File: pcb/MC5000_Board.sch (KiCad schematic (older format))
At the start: 0 parts

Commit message: Work on PCB
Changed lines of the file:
@@
 $Descr A4 11693 8268
 encoding utf-8
-Sheet 1 9
+Sheet 1 10
 Title ""
 Date ""
@@
 $EndSheet
 $Sheet
-S 750  750  1750 1100
+S 2650 3700 1600 1050
 U 602FB936
-F0 "PFS172 breakout - Display Controller" 50
+F0 "PFS172 breakout - Display Ctrl" 50
 F1 "PFS172_breakout.sch" 50
 $EndSheet
 $Sheet
-S 2850 750  1600 1100
+S 750  750  1600 1100
 U 60303416
 F0 "PFS172 breakout - MCU1" 50
@@
 $EndSheet
 $Sheet
-S 750  2200 1750 1050
+S 2650 800  1600 1050
 U 6030344A
 F0 "PFS172 breakout - MCU2" 50
@@
 $EndSheet
 $Sheet
-S 2850 2200 1600 1050
+S 750  2200 1600 1050
 U 603034BC
 F0 "PFS172 breakout - MCU3" 50
@@
 $EndSheet
 $Sheet
-S 750  3700 1750 1050
+S 750  3700 1600 1050
 U 60318BF9
-F0 "PFS172 extra #1" 50
+F0 "PFS172 Buzzer Ctrl" 50
 F1 "PFS172_breakout.sch" 50
 $EndSheet
 $Sheet
-S 2850 3700 1600 1050
+S 2650 2200 1600 1050
 U 60318BFB
-F0 "PFS172 extra #2" 50
+F0 "PFS172 extra" 50
 F1 "PFS172_breakout.sch" 50
 $EndSheet
+$Sheet
+S 800  6400 1550 1050
+U 6034DF24
+F0 "MCU5000 #1" 50
+F1 "MCU5000.sch" 50
+$EndSheet
 $EndSCHEMATC

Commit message: Added buzzer
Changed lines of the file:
@@
 $Descr A4 11693 8268
 encoding utf-8
-Sheet 1 10
+Sheet 1 12
 Title ""
 Date ""
@@
 F1 "MCU5000.sch" 50
 $EndSheet
+$Sheet
+S 2700 6400 1550 1050
+U 603599D1
+F0 "MCU5000 #2" 50
+F1 "MCU5000.sch" 50
+$EndSheet
+$Sheet
+S 8500 700  1700 1000
+U 603632C9
+F0 "Buzzer" 50
+F1 "buzzer.sch" 50
+$EndSheet
 $EndSCHEMATC

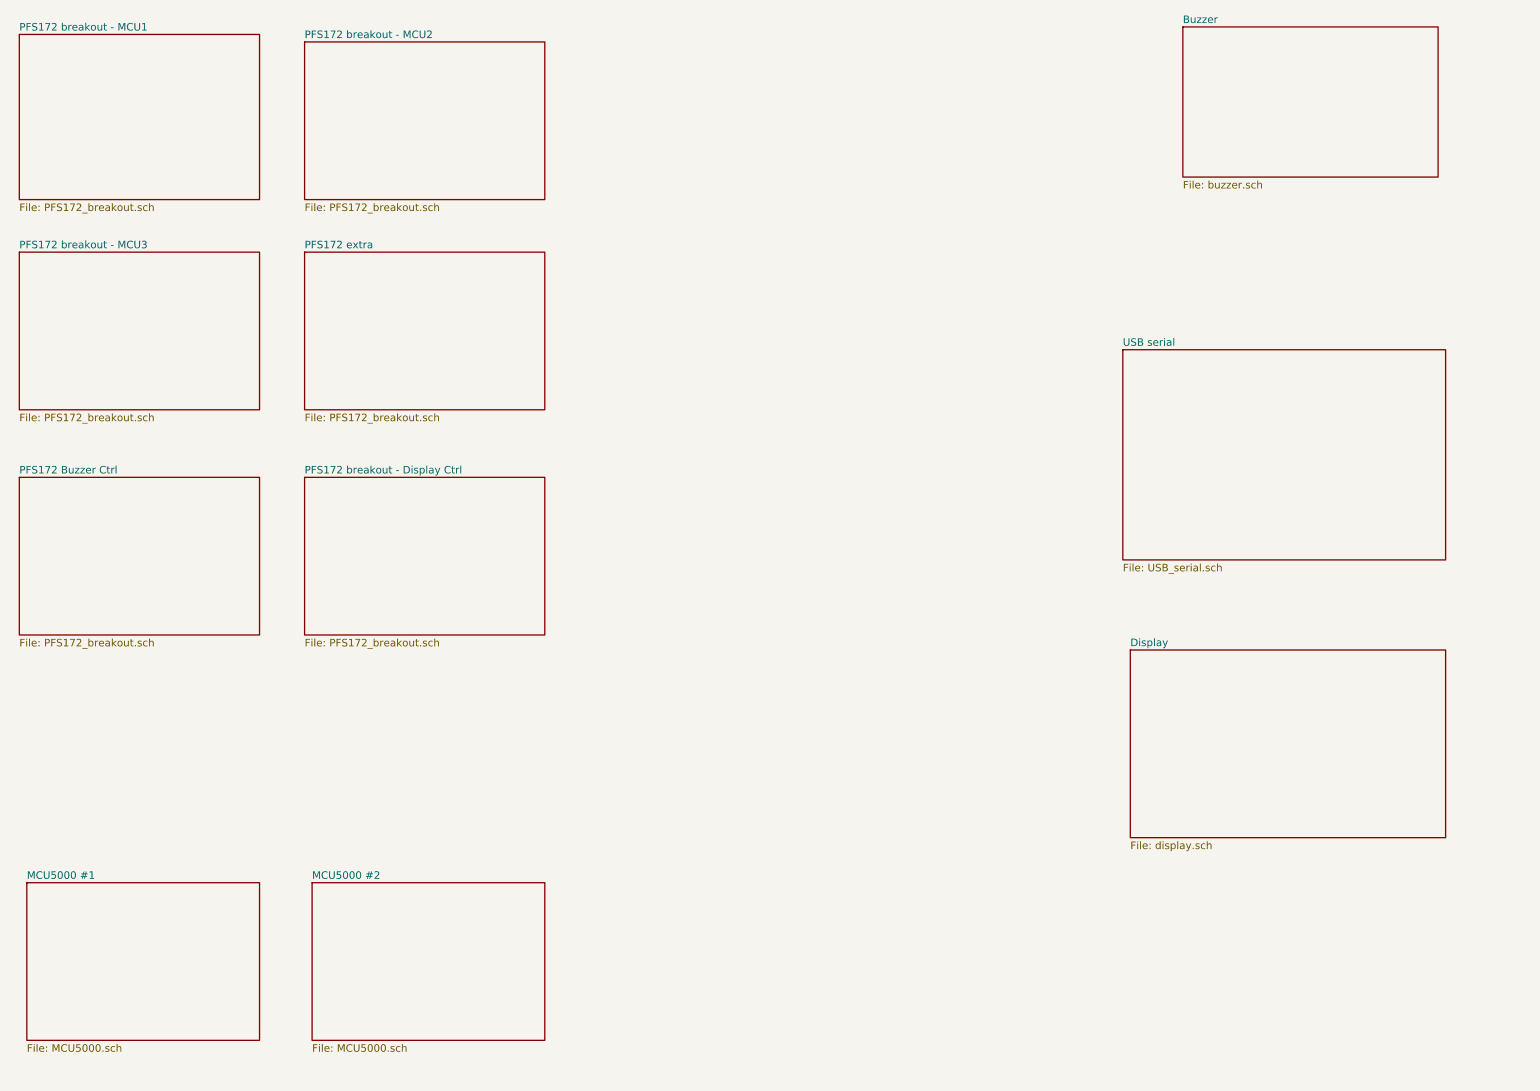
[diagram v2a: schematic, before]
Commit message: Added LEDs
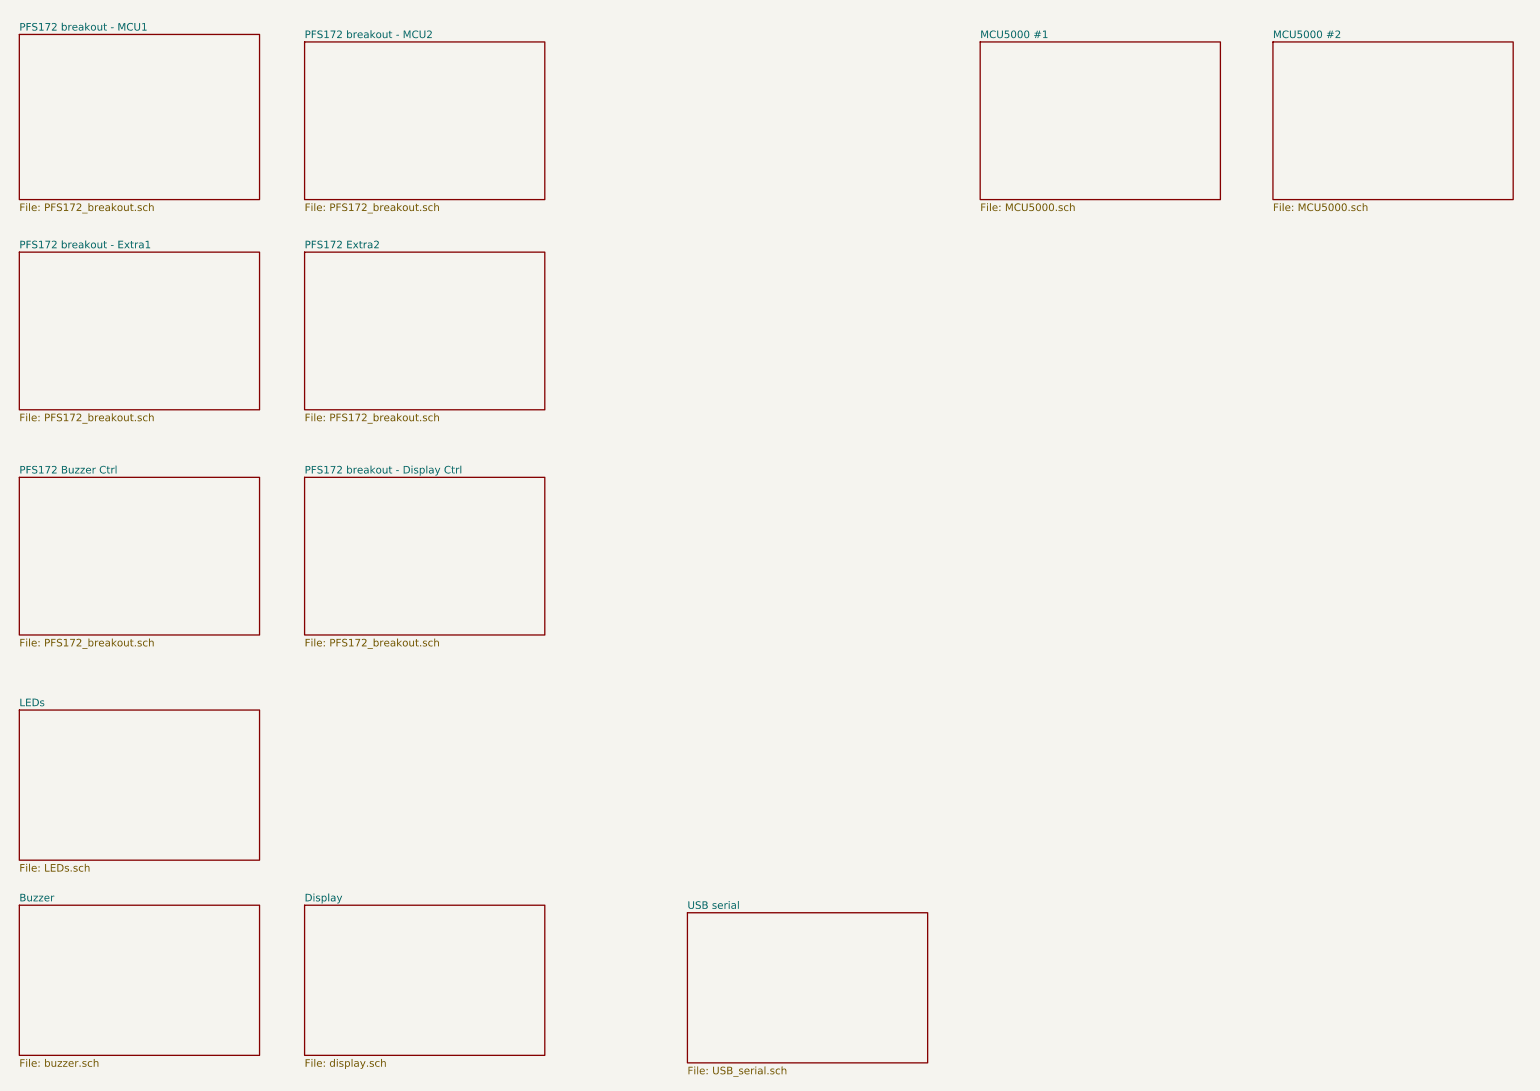
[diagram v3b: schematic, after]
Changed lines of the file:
@@
 $Descr A4 11693 8268
 encoding utf-8
-Sheet 1 12
+Sheet 1 13
 Title ""
 Date ""
@@
 $EndDescr
 $Sheet
-S 8100 2850 2150 1400
+S 5200 6600 1600 1000
 U 602FF29A
 F0 "USB serial" 50
@@
 S 750  2200 1600 1050
 U 603034BC
-F0 "PFS172 breakout - MCU3" 50
+F0 "PFS172 breakout - Extra1" 50
 F1 "PFS172_breakout.sch" 50
 $EndSheet
 $Sheet
-S 8150 4850 2100 1250
+S 2650 6550 1600 1000
 U 60308700
 F0 "Display" 50
@@
 S 2650 2200 1600 1050
 U 60318BFB
-F0 "PFS172 extra" 50
+F0 "PFS172 Extra2" 50
 F1 "PFS172_breakout.sch" 50
 $EndSheet
 $Sheet
-S 800  6400 1550 1050
+S 7150 800  1600 1050
 U 6034DF24
 F0 "MCU5000 #1" 50
@@
 $EndSheet
 $Sheet
-S 2700 6400 1550 1050
+S 9100 800  1600 1050
 U 603599D1
 F0 "MCU5000 #2" 50
@@
 $EndSheet
 $Sheet
-S 8500 700  1700 1000
+S 750  6550 1600 1000
 U 603632C9
 F0 "Buzzer" 50
 F1 "buzzer.sch" 50
 $EndSheet
+$Sheet
+S 750  5250 1600 1000
+U 6036720E
+F0 "LEDs" 50
+F1 "LEDs.sch" 50
+$EndSheet
 $EndSCHEMATC

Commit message: Added switches
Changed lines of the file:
@@
 $Descr A4 11693 8268
 encoding utf-8
-Sheet 1 13
+Sheet 1 15
 Title ""
 Date ""
@@
 F1 "LEDs.sch" 50
 $EndSheet
+$Sheet
+S 9100 2200 1600 1000
+U 603926D8
+F0 "Switch #2" 50
+F1 "switch.sch" 50
+$EndSheet
+$Sheet
+S 7150 2200 1600 1000
+U 6037B4F8
+F0 "Switches" 50
+F1 "switches.sch" 50
+$EndSheet
 $EndSCHEMATC

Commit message: Changes
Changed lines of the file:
@@
 $Descr A4 11693 8268
 encoding utf-8
-Sheet 1 15
+Sheet 1 14
 Title ""
 Date ""
@@
 $EndSheet
 $Sheet
-S 9100 2200 1600 1000
-U 603926D8
-F0 "Switch #2" 50
-F1 "switch.sch" 50
-$EndSheet
-$Sheet

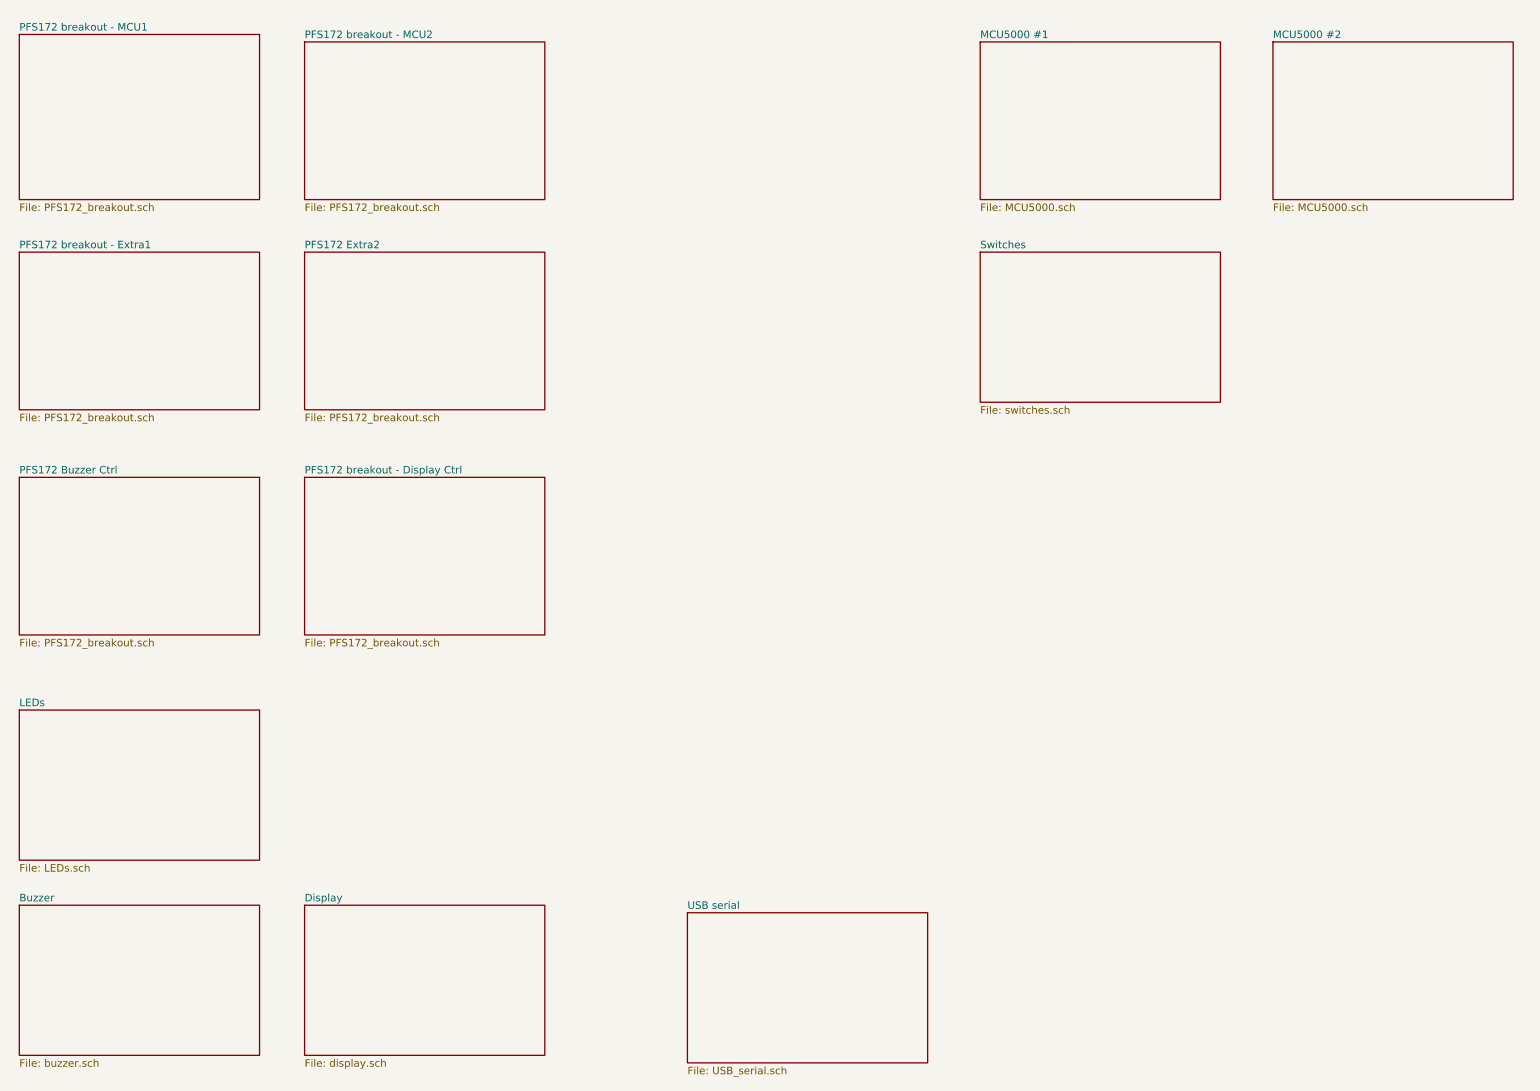
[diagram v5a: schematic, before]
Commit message: changed pcb file structure
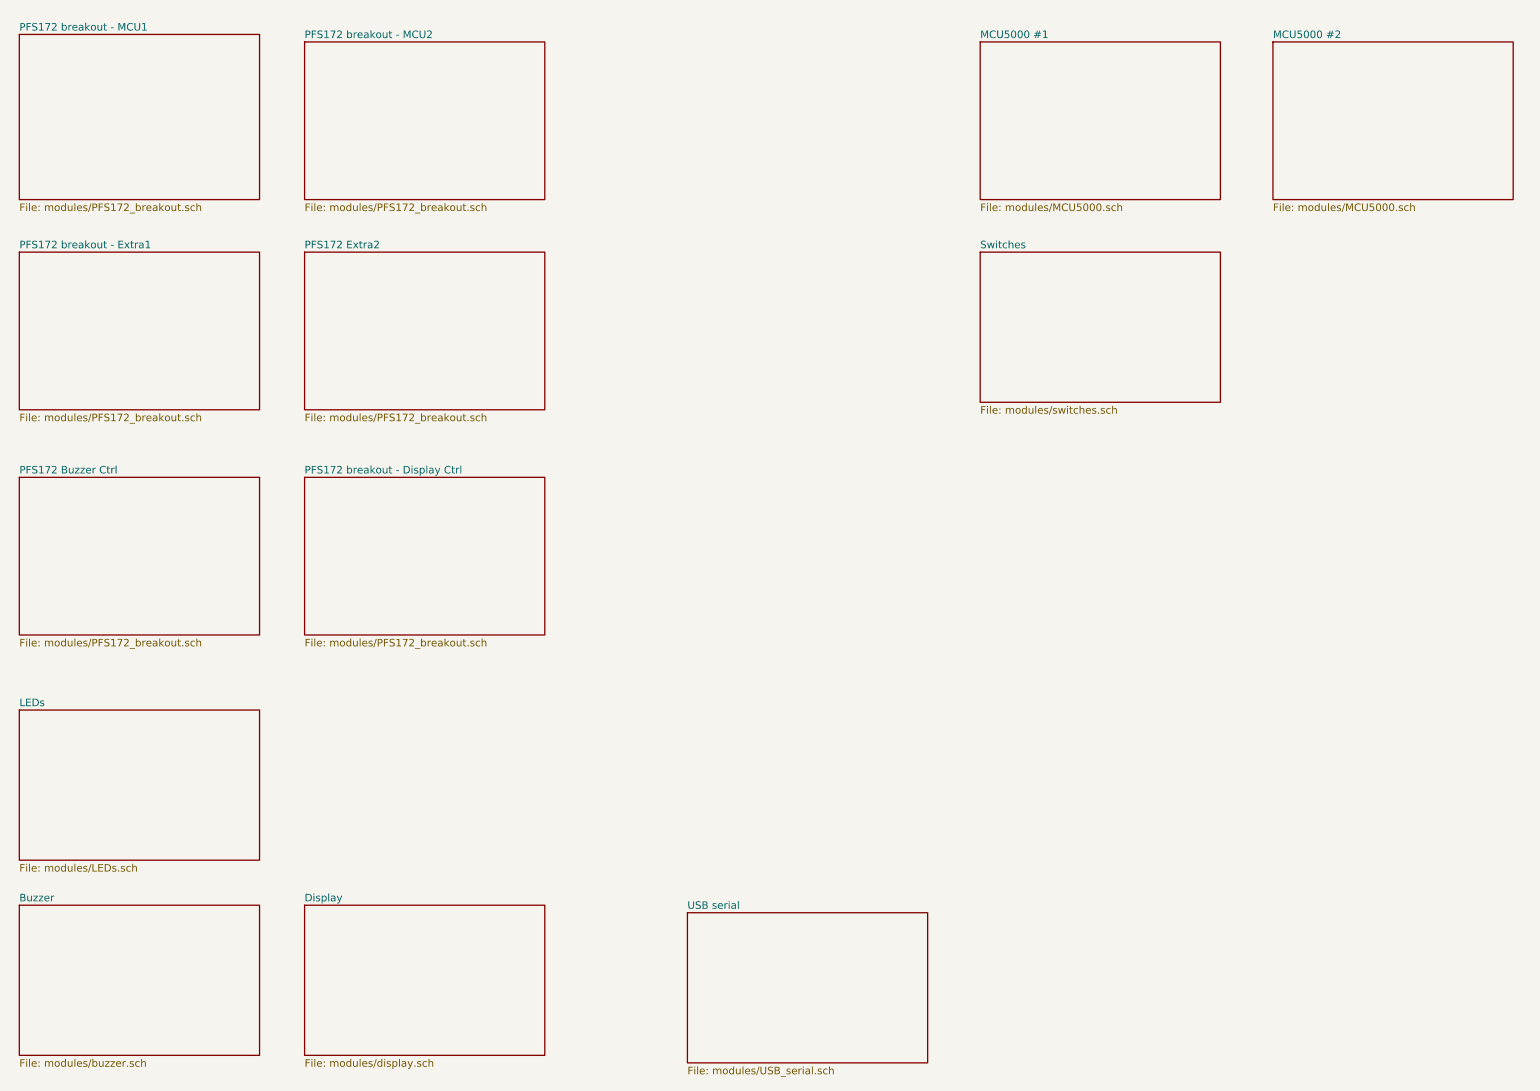
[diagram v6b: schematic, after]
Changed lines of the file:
@@
 U 602FF29A
 F0 "USB serial" 50
-F1 "USB_serial.sch" 50
+F1 "modules/USB_serial.sch" 50
 $EndSheet
 $Sheet
@@
 U 602FB936
 F0 "PFS172 breakout - Display Ctrl" 50
-F1 "PFS172_breakout.sch" 50
+F1 "modules/PFS172_breakout.sch" 50
 $EndSheet
 $Sheet
@@
 U 60303416
 F0 "PFS172 breakout - MCU1" 50
-F1 "PFS172_breakout.sch" 50
+F1 "modules/PFS172_breakout.sch" 50
 $EndSheet
 $Sheet
@@
 U 6030344A
 F0 "PFS172 breakout - MCU2" 50
-F1 "PFS172_breakout.sch" 50
+F1 "modules/PFS172_breakout.sch" 50
 $EndSheet
 $Sheet
@@
 U 603034BC
 F0 "PFS172 breakout - Extra1" 50
-F1 "PFS172_breakout.sch" 50
+F1 "modules/PFS172_breakout.sch" 50
 $EndSheet
 $Sheet
@@
 U 60308700
 F0 "Display" 50
-F1 "display.sch" 50
+F1 "modules/display.sch" 50
 $EndSheet
 $Sheet
@@
 U 60318BF9
 F0 "PFS172 Buzzer Ctrl" 50
-F1 "PFS172_breakout.sch" 50
+F1 "modules/PFS172_breakout.sch" 50
 $EndSheet
 $Sheet
@@
 U 60318BFB
 F0 "PFS172 Extra2" 50
-F1 "PFS172_breakout.sch" 50
+F1 "modules/PFS172_breakout.sch" 50
 $EndSheet
 $Sheet
@@
 U 6034DF24
 F0 "MCU5000 #1" 50
-F1 "MCU5000.sch" 50
+F1 "modules/MCU5000.sch" 50
 $EndSheet
 $Sheet
@@
 U 603599D1
 F0 "MCU5000 #2" 50
-F1 "MCU5000.sch" 50
+F1 "modules/MCU5000.sch" 50
 $EndSheet
 $Sheet
@@
 U 603632C9
 F0 "Buzzer" 50
-F1 "buzzer.sch" 50
+F1 "modules/buzzer.sch" 50
 $EndSheet
 $Sheet
@@
 U 6036720E
 F0 "LEDs" 50
-F1 "LEDs.sch" 50
+F1 "modules/LEDs.sch" 50
 $EndSheet
 $Sheet
@@
 U 6037B4F8
 F0 "Switches" 50
-F1 "switches.sch" 50
+F1 "modules/switches.sch" 50
 $EndSheet
 $EndSCHEMATC

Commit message: finished pcb
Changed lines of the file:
@@
 $Descr A4 11693 8268
 encoding utf-8
-Sheet 1 14
+Sheet 1 17
 Title ""
 Date ""
@@
 $EndDescr
 $Sheet
-S 5200 6600 1600 1000
+S 5000 6450 1600 1000
 U 602FF29A
 F0 "USB serial" 50
@@
 $EndSheet
 $Sheet
-S 2650 6550 1600 1000
+S 9050 800  1600 1000
 U 60308700
 F0 "Display" 50
@@
 $EndSheet
 $Sheet
-S 7150 800  1600 1050
+S 700  6450 1600 1050
 U 6034DF24
 F0 "MCU5000 #1" 50
@@
 $EndSheet
 $Sheet
-S 9100 800  1600 1050
+S 2650 6450 1600 1050
 U 603599D1
 F0 "MCU5000 #2" 50
@@
 $EndSheet
 $Sheet
-S 750  6550 1600 1000
+S 7150 800  1600 1000
 U 603632C9
 F0 "Buzzer" 50
@@
 $EndSheet
 $Sheet
-S 750  5250 1600 1000
+S 7150 2150 1600 1000
 U 6036720E
 F0 "LEDs" 50
@@
 $EndSheet
 $Sheet
-S 7150 2200 1600 1000
+S 7150 5200 1600 1000
 U 6037B4F8
 F0 "Switches" 50
 F1 "modules/switches.sch" 50
 $EndSheet
+$Sheet
+S 9200 5200 1600 1000
+U 6038A837
+F0 "Temp sensor" 50
+F1 "modules/temp_sensor.sch" 50
+$EndSheet
+$Sheet
+S 9200 3700 1600 1050
+U 6038ECB3
+F0 "Light sensor" 50
+F1 "modules/light_sensor.sch" 50
+$EndSheet
+$Sheet
+S 5000 3700 1600 1050
+U 603839E8
+F0 "Connection block" 50
+F1 "connection_block.sch" 50
+$EndSheet
 $EndSCHEMATC

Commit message: Production board
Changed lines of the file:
@@
 $Descr A4 11693 8268
 encoding utf-8
-Sheet 1 17
+Sheet 1 11
 Title ""
 Date ""
@@
 $EndSheet
 $Sheet
-S 2650 3700 1600 1050
-U 602FB936
-F0 "PFS172 breakout - Display Ctrl" 50
-F1 "modules/PFS172_breakout.sch" 50
-$EndSheet
-$Sheet
-S 750  750  1600 1100
-U 60303416
-F0 "PFS172 breakout - MCU1" 50
-F1 "modules/PFS172_breakout.sch" 50
-$EndSheet
-$Sheet
-S 2650 800  1600 1050
-U 6030344A
-F0 "PFS172 breakout - MCU2" 50
-F1 "modules/PFS172_breakout.sch" 50
-$EndSheet
-$Sheet
-S 750  2200 1600 1050
-U 603034BC
-F0 "PFS172 breakout - Extra1" 50
-F1 "modules/PFS172_breakout.sch" 50
-$EndSheet
-$Sheet
 S 9050 800  1600 1000
 U 60308700
 F0 "Display" 50
 F1 "modules/display.sch" 50
-$EndSheet
-$Sheet
-S 750  3700 1600 1050
-U 60318BF9
-F0 "PFS172 Buzzer Ctrl" 50
-F1 "modules/PFS172_breakout.sch" 50
-$EndSheet
-$Sheet
-S 2650 2200 1600 1050
-U 60318BFB
-F0 "PFS172 Extra2" 50
-F1 "modules/PFS172_breakout.sch" 50
 $EndSheet
 $Sheet
@@
 $EndSheet
 $Sheet
-S 5000 3700 1600 1050
+S 900  850  1600 1050
 U 603839E8
 F0 "Connection block" 50
